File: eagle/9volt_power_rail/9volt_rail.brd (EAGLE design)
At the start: 94.9 x 67.3 mm, 48 parts, among them IC1 TL331

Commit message: Done with power board and adc cape
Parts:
- removed T1, T3: (no value), zetex:SOT223
- added H1, H2, H3, H4: MOUNT-PAD-ROUND3.0, holes:3,0-PAD
- added Q1: BSS84, transistor-small-signal:SOT23
- added Q2: BSS123, transistor-small-signal:SOT23
- added R12: (no value), adafruit:M0805
- moved R10 8.58 mm to (75.6, 20.2), turned to 270 degrees
- moved VCC1 7.21 mm to (1.59, 3.02), turned to 0 degrees
- moved VCC2 7.21 mm to (1.59, 63.7)
- moved C3 4.77 mm to (67.8, 20.6), turned to 270 degrees
- moved VCC3 0.97 mm to (1.75, 48.1)
- moved R11 0.16 mm to (8.10, 44.8), flipped to the bottom, turned to 0 degrees
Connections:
- net GND: now also H1.B3,0, H2.B3,0, H3.B3,0, H4.B3,0, Q2.2, R12.2; no longer T3.2, T3.4
- net N$10: now also Q2.3, U$3.3; no longer R11.1, T1.2, T1.4
- net N$2: now also Q1.1; no longer T1.1, T3.1
- net N$5: now also Q1.3, Q2.1, R11.1, R12.1; no longer T3.3, U$3.3
- net VCC: now also Q1.2; no longer T1.3
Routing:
- net N$10: track 64.0 -> 12.7 mm
- net N$5: track 17.5 -> 58.2 mm, vias 1 -> 0
- net VCC: track 75.2 -> 65.7 mm
- net N$3: track 12.0 -> 20.8 mm
- net N$2: track 47.1 -> 53.1 mm
- net N$9: track 4.63 -> 10.3 mm
- net N$8: track 4.65 -> 6.46 mm
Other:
- board size 94.9 x 67.3 mm -> 98.3 x 69.5 mm

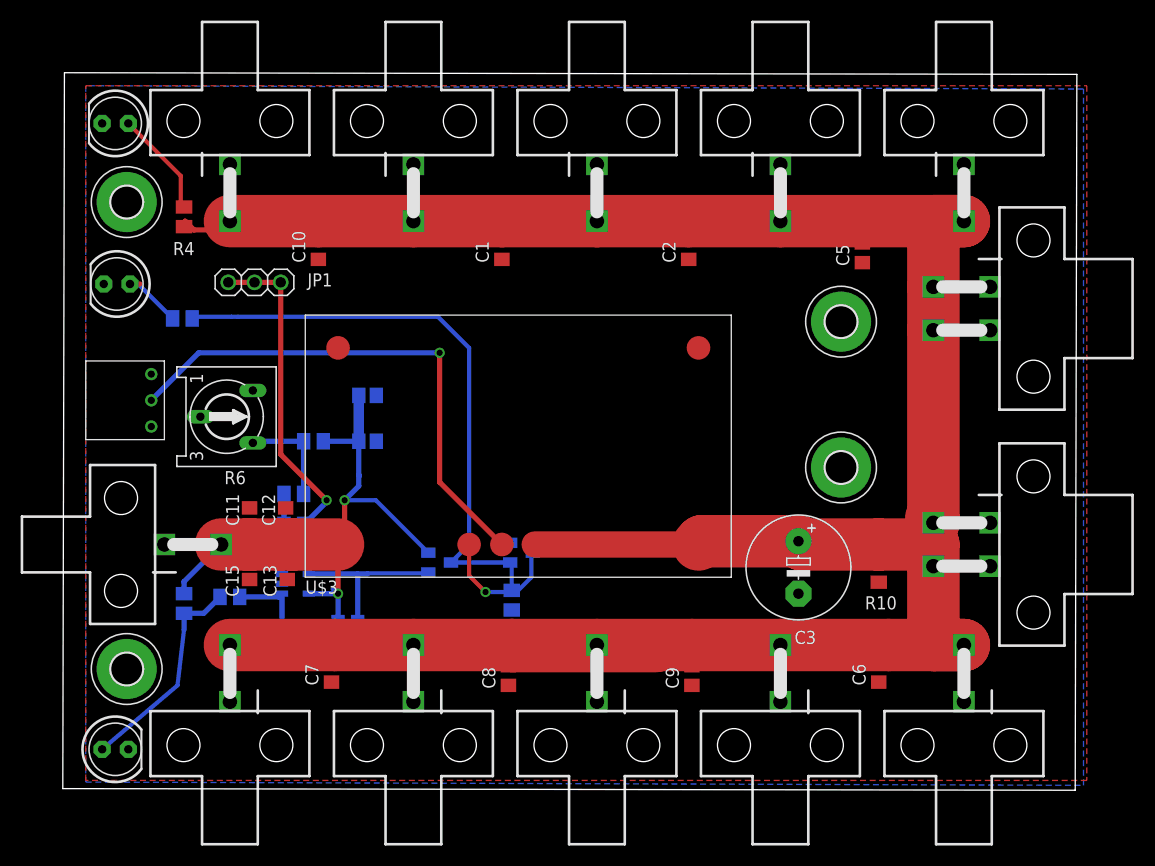
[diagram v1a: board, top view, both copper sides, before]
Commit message: update to adc cape
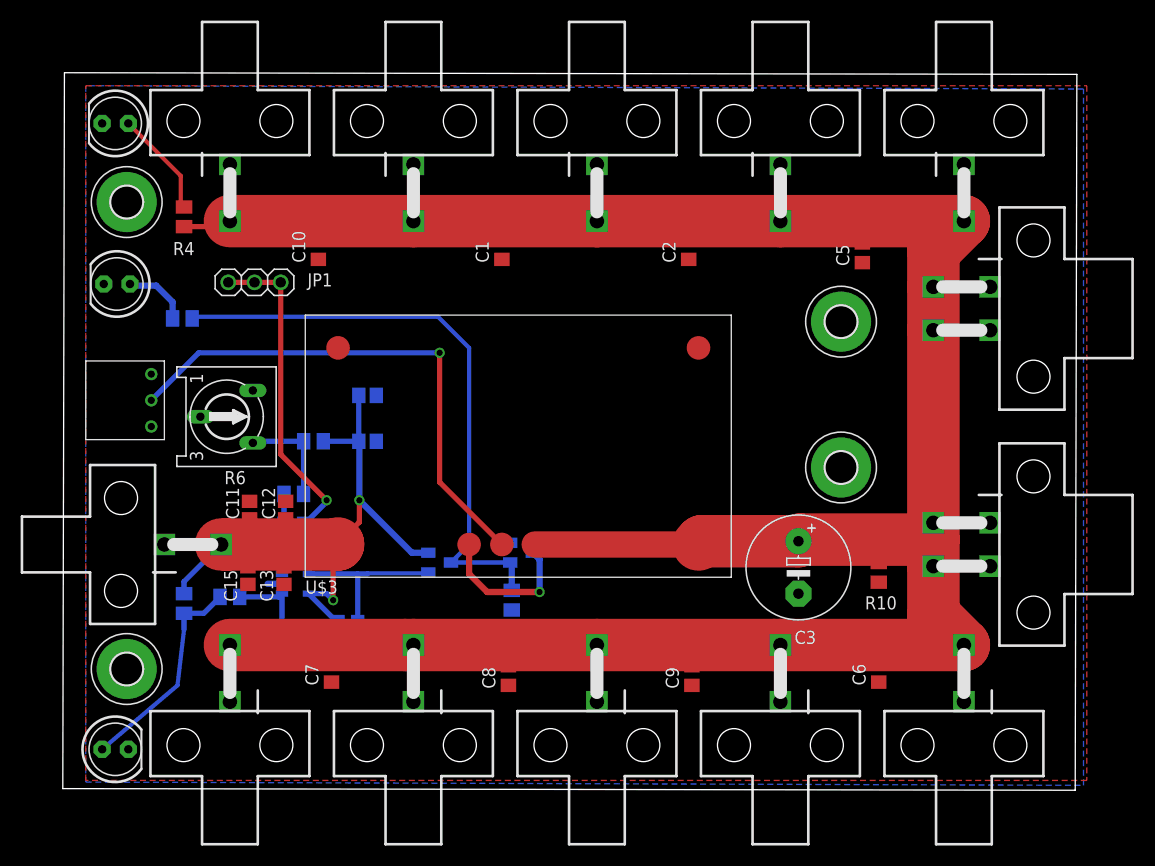
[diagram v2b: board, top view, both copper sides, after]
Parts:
- moved C11 0.64 mm to (14.6, 26.2)
- moved C12 0.64 mm to (18.1, 26.2)
- moved C13 0.57 mm to (17.9, 19.8)
- moved C15 0.50 mm to (14.4, 19.8)
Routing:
- net N$11: track 273.3 -> 301.7 mm
- net VCC: track 65.7 -> 78.4 mm
- net N$10: track 12.7 -> 14.5 mm
- net GND: track 0.00 -> 1.39 mm
